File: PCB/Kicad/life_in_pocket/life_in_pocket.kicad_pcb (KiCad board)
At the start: 2 copper layers, 121.7 x 77.3 mm, 62 parts, among them J2 USB_C_Receptacle_USB2.0_16P, Q1 QM6015D, SW1 SW_SPST, SW2 Switch, SW3 Switch, SW4 Switch, SW5 Switch, U1 ESP32-S3-WROOM-1, U2 Adafruit I2S 3W Class D Ampli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, U3 MicroSd breakout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

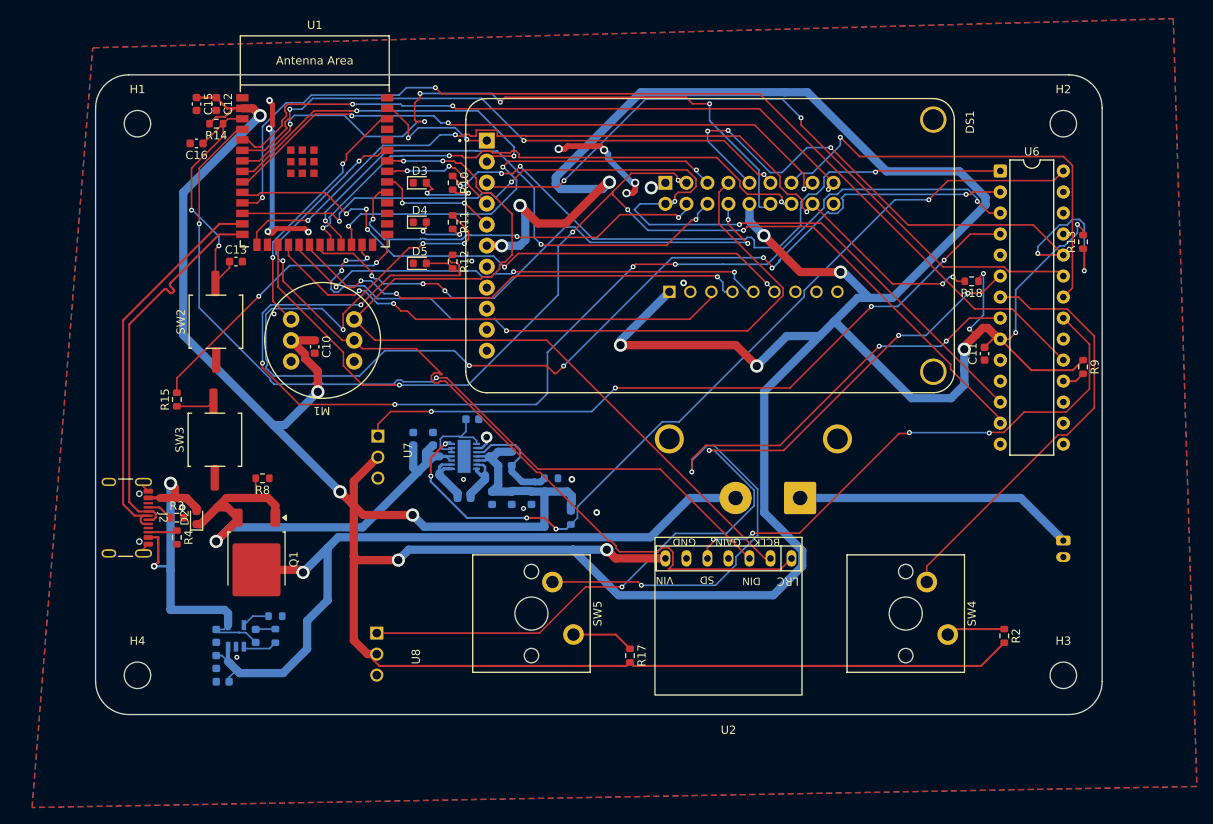
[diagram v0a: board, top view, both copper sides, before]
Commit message: Changed pcb's components to THT (top side only) for cheaper assembly
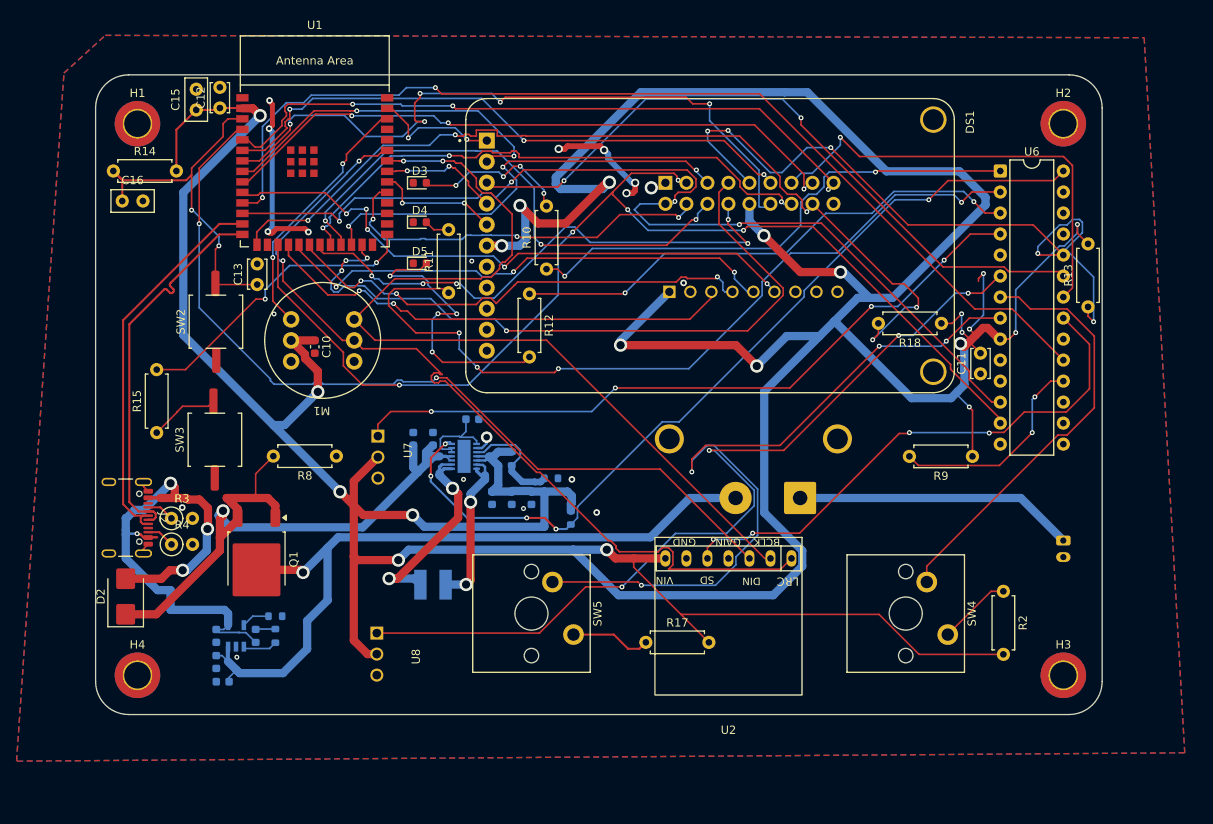
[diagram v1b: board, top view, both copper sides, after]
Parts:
- C11, C12, C13: footprint Capacitor_SMD:C_0603_1608Metric -> Capacitor_THT:C_Disc_D3.4mm_W2.1mm_P2.50mm
- C15, C16: footprint Capacitor_SMD:C_0603_1608Metric -> Capacitor_THT:C_Disc_D5.0mm_W2.5mm_P2.50mm
- D2: footprint Diode_SMD:D_0603_1608Metric -> Diode_SMD:D_SMB
- H1, H2, H3, H4: footprint MountingHole:MountingHole_3.2mm_M3 -> MountingHole:MountingHole_3.2mm_M3_ISO14580_Pad_TopBottom
- L1: footprint Inductor_SMD:L_0603_1608Metric -> Inductor_SMD:L_Bourns-SRN4018
- R10, R11, R12, R13, R14, R15, R17, R18, R2, R8, R9: footprint Resistor_SMD:R_0603_1608Metric -> Resistor_THT:R_Axial_DIN0207_L6.3mm_D2.5mm_P7.62mm_Horizontal
- R3, R4: footprint Resistor_SMD:R_0603_1608Metric -> Resistor_THT:R_Axial_DIN0207_L6.3mm_D2.5mm_P2.54mm_Vertical
- moved R9 17.2 mm to (191.4, 90.2), turned to 180 degrees
- moved R10 15.4 mm to (139.9, 67.6), turned to 90 degrees
- moved R14 13.7 mm to (87.6, 55.7), turned to 0 degrees
- moved D2 12.8 mm to (89.1, 107.2)
- moved C16 11.4 mm to (88.7, 59.4), turned to 0 degrees
- moved L1 11.1 mm to (126.2, 105.7)
- moved R12 10.1 mm to (137.9, 70.6)
- moved R8 9.32 mm to (114.5, 90.2)
- moved R11 8.54 mm to (128.1, 70.4), turned to 90 degrees
- moved R13 7.88 mm to (205.4, 72.2)
- moved R18 6.26 mm to (187.7, 74.1)
- moved R2 5.39 mm to (195.2, 106.5)
- moved R15 4.69 mm to (92.8, 87.3)
- moved C13 3.78 mm to (105.0, 69.5), turned to 90 degrees
- moved R17 2.50 mm to (151.9, 112.7), turned to 0 degrees
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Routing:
- net Net-(U6-GPB2): track 142.6 -> 63.1 mm, vias 6 -> 2
- net Net-(U6-GPB1): track 145.0 -> 98.3 mm, vias 8 -> 4
- net Net-(D5-A): track 3.44 -> 34.9 mm, vias 0 -> 4
- net Net-(U6-~{RESET}): track 2.75 -> 25.6 mm, vias 0 -> 2
- net VBUS: track 46.8 -> 67.4 mm, vias 2 -> 4
- net Net-(L1-Pad1): track 7.91 -> 25.8 mm, vias 0 -> 2
- net Net-(D2-K): track 62.3 -> 80.1 mm
- net Net-(U6-GPB0): track 78.9 -> 62.8 mm, vias 4 -> 2
- net 3.3V: track 601.6 -> 585.7 mm, vias 18 -> 21
- net Net-(L1-Pad2): track 7.12 -> 20.3 mm, vias 0 -> 2
- net EN: track 31.8 -> 44.4 mm
- net Net-(D3-A): track 9.34 -> 19.0 mm, vias 2 -> 4
- net PWDN: track 79.7 -> 87.3 mm
- net D5: track 103.9 -> 108.8 mm
- net Net-(D4-A): track 6.96 -> 3.08 mm, vias 2 -> 0
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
